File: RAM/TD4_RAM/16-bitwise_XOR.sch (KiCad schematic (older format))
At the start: 16 parts, among them U45 74HC86, U46 74HC86, U47 74HC86, U48 74HC86, U49 74HC86, U50 74HC86, U51 74HC86, U52 74HC86

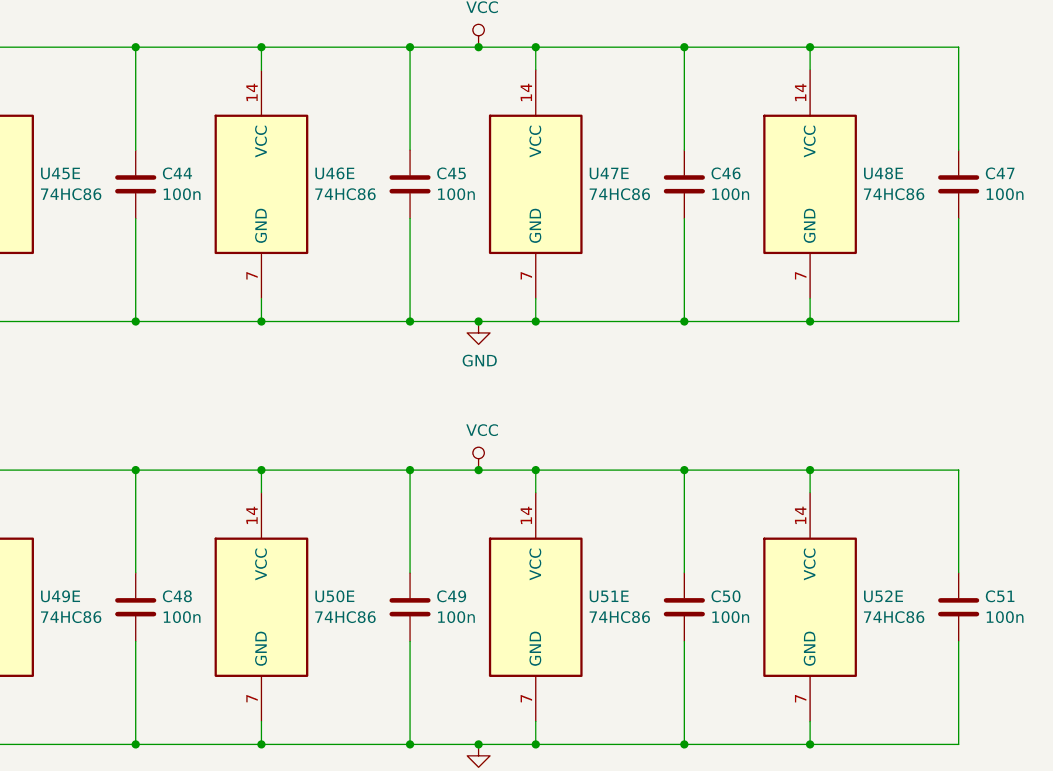
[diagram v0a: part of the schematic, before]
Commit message: Added backplane connectors to all PCBs
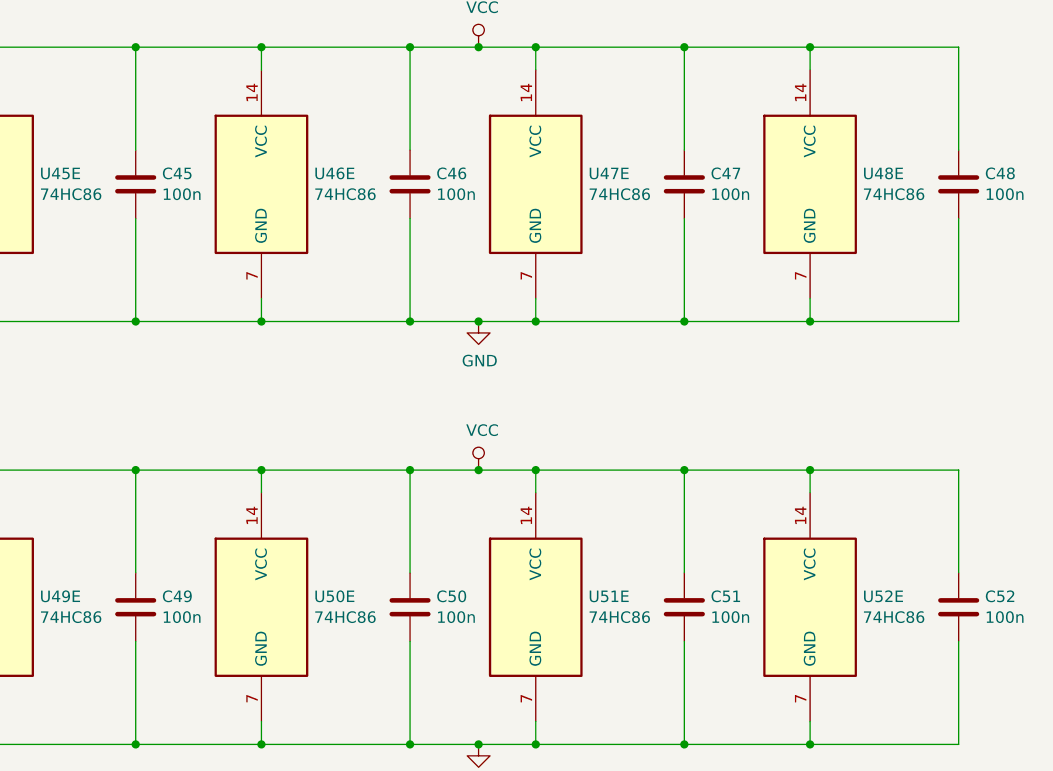
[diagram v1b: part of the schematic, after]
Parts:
- C45: renamed from C44; footprint (none) -> Capacitor_SMD:C_0805_2012Metric
- C46: renamed from C45; footprint (none) -> Capacitor_SMD:C_0805_2012Metric
- C47: renamed from C46; footprint (none) -> Capacitor_SMD:C_0805_2012Metric
- C48: renamed from C47; footprint (none) -> Capacitor_SMD:C_0805_2012Metric
- C49: renamed from C48; footprint (none) -> Capacitor_SMD:C_0805_2012Metric
- C50: renamed from C49; footprint (none) -> Capacitor_SMD:C_0805_2012Metric
- C51: renamed from C50; footprint (none) -> Capacitor_SMD:C_0805_2012Metric
- C52: renamed from C51; footprint (none) -> Capacitor_SMD:C_0805_2012Metric
- U45, U46, U47, U48, U49, U50, U51, U52: footprint (none) -> Package_SO:SOIC-14_3.9x8.7mm_P1.27mm

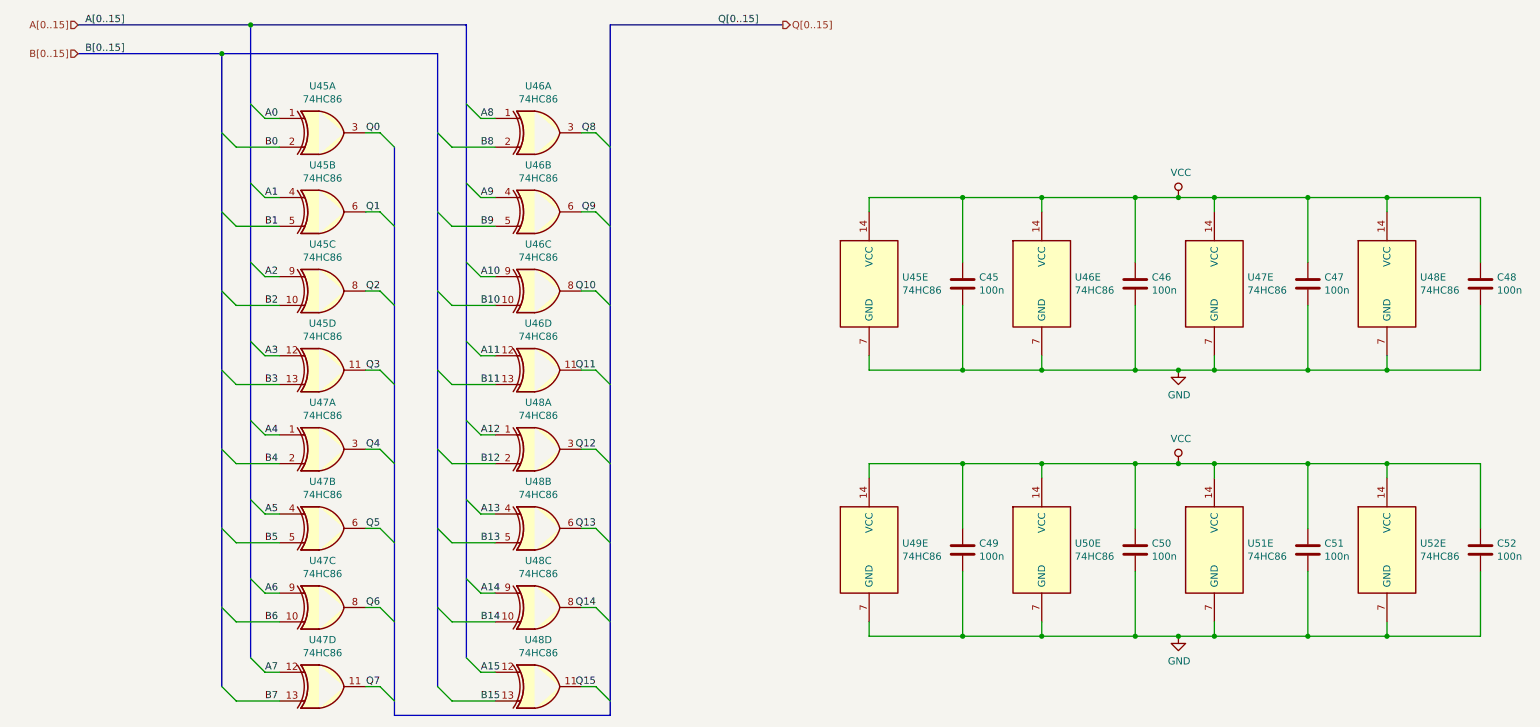
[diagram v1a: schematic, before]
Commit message: Main RAM blocks routed
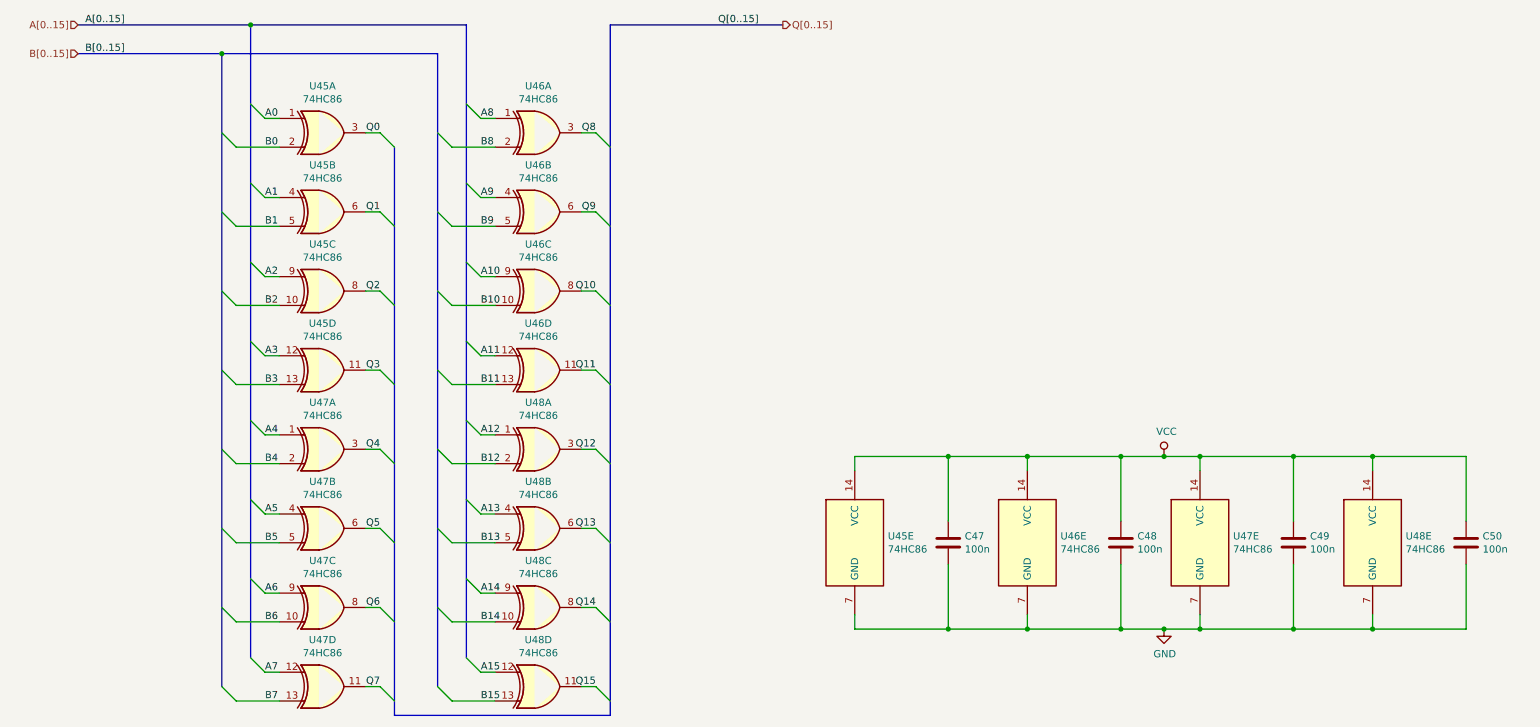
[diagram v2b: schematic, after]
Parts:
- removed C49, C50, C51, C52: 100n, Capacitor_SMD:C_0805_2012Metric, symbol Device:C
- removed U49, U50, U51, U52: 74HC86, Package_SO:SOIC-14_3.9x8.7mm_P1.27mm, symbol 74xx:74HC86
- renumbered C45 to C47, C46 to C48, C47 to C49, C48 to C50
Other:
- moved on the sheet: C47, C48, C49, C50, U45E, U46E, U47E, U48E
